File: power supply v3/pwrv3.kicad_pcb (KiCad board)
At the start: 2 copper layers, 38.3 x 37.5 mm, 56 parts, among them IC1 TLV3701IDBVR, IC2 LM25145RGYR, IC3 LMR50410YQDBVRQ1, J1 1.5 mm, J3 1933189, J4 Conn_01x04_Pin 1.27mm, Q1 35A, 30V, Q2 35A Id, 30V Vds

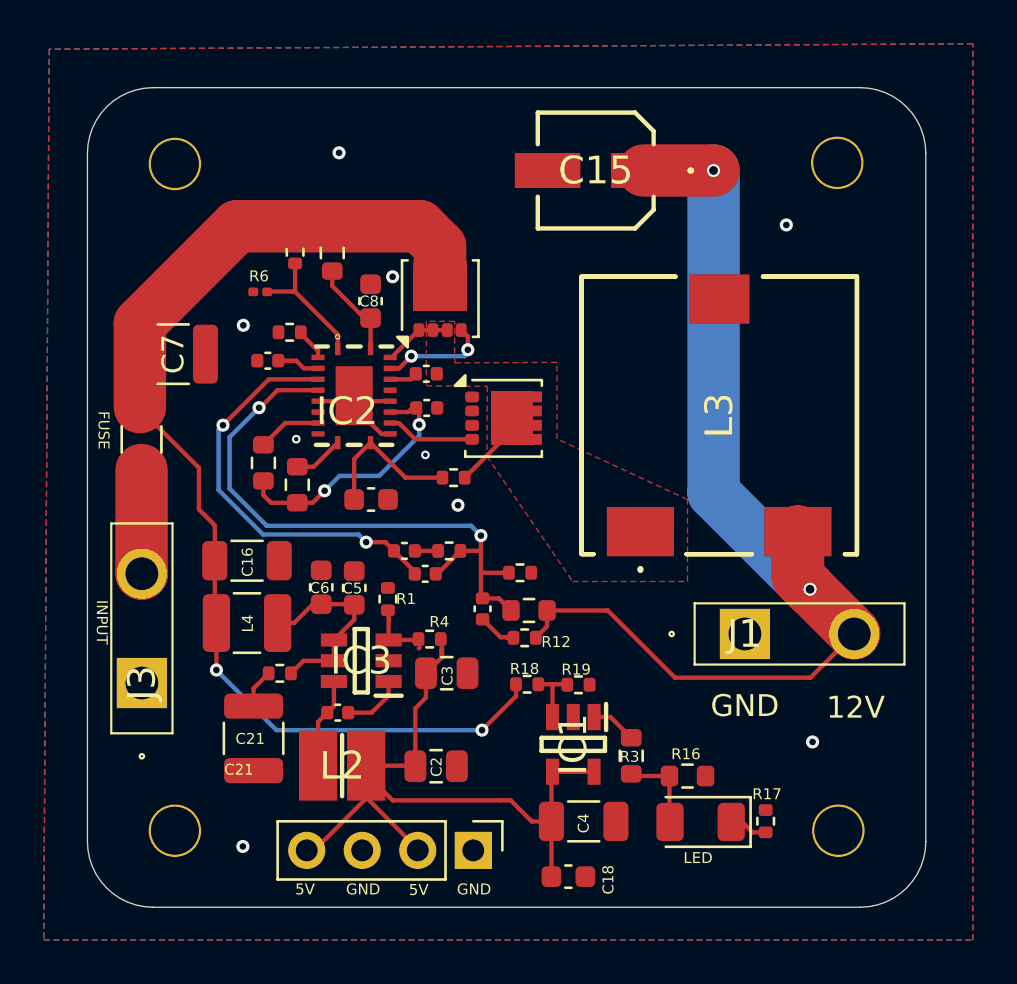
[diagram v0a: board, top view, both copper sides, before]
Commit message: capa bst updated
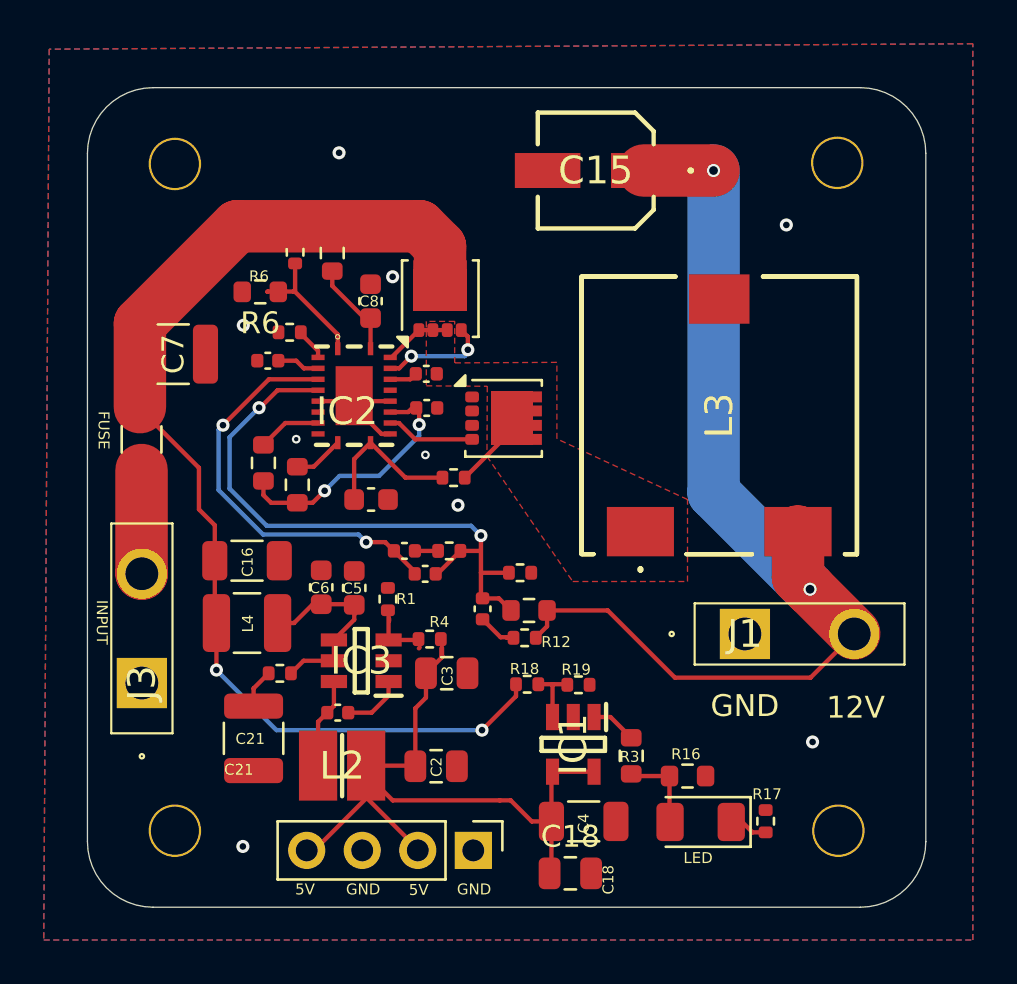
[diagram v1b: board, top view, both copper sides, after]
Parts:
- C17: value GCM1555C1H100FA16D -> 0.1uF
- C18: footprint Capacitor_SMD:C_0603_1608Metric -> Capacitor_SMD:C_0805_2012Metric
- R18: value R -> 30.9k
- R19: value R -> 22.1k
- R6: footprint Resistor_SMD:R_0201_0603Metric -> Resistor_SMD:R_0603_1608Metric
- moved C18 0.17 mm to (186.1, 110.0)
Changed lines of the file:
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@@
 			(disableapertmacros no)
 			(usegerberextensions yes)
-			(usegerberattributes yes)
-			(usegerberadvancedattributes yes)
+			(usegerberattributes no)
+			(usegerberadvancedattributes no)
 			(creategerberjobfile no)
 			(dashed_line_dash_ratio 12.000000)
@@
 			(drillshape 0)
 			(scaleselection 1)
-			(outputdirectory "gerber files/")
+			(outputdirectory "gerbers/")
 		)
 	)
@@
 			)
 		)
-		(property "Value" "R"
+		(property "Value" "22.1k"
 			(at 0 1.17 0)
 			(layer "F.Fab")
@@
 		)
 	)
-	(footprint "Resistor_SMD:R_0201_0603Metric"
+	(footprint "Resistor_SMD:R_0603_1608Metric"
 		(layer "F.Cu")
 		(at 171.905 83.35 180)
-		(descr "Resistor SMD 0201 (0603 Metric), square (rectangular) end terminal, IPC_7351 nominal, (Body size source: https://www.vishay.com/docs/20052/crcw0201e3.pdf), generated with kicad-footprint-generator")
+		(descr "Resistor SMD 0603 (1608 Metric), square (rectangular) end terminal, IPC_7351 nominal, (Body size source: IPC-SM-782 page 72, https://www.pcb-3d.com/wordpress/wp-content/uploads/ipc-sm-782a_amendment_1_and_2.pdf), generated with kicad-footprint-generator")
 		(tags "resistor")
 		(property "Reference" "R6"
-			(at 0 -1.05 0)
+			(at 0 -1.43 180)
 			(layer "F.SilkS")
-			(hide yes)
 			(effects
 				(font
@@
 		)
 		(property "Value" "8.25k"
-			(at 0 1.05 0)
+			(at 0 1.43 180)
 			(layer "F.Fab")
 			(effects
@@
 		(attr smd)
 		(fp_line
-			(start 0.7 0.35)
-			(end -0.7 0.35)
+			(start -0.237258 0.5225)
+			(end 0.237258 0.5225)
+			(stroke
+				(width 0.12)
+				(type solid)
+			)
+			(layer "F.SilkS")
+		)
+		(fp_line
+			(start -0.237258 -0.5225)
+			(end 0.237258 -0.5225)
+			(stroke
+				(width 0.12)
+				(type solid)
+			)
+			(layer "F.SilkS")
+		)
+		(fp_line
+			(start 1.48 0.73)
+			(end -1.48 0.73)
 			(stroke
 				(width 0.05)
@@
 		)
 		(fp_line
-			(start 0.7 -0.35)
-			(end 0.7 0.35)
+			(start 1.48 -0.73)
+			(end 1.48 0.73)
 			(stroke
 				(width 0.05)
@@
 		)
 		(fp_line
-			(start -0.7 0.35)
-			(end -0.7 -0.35)
+			(start -1.48 0.73)
+			(end -1.48 -0.73)
 			(stroke
 				(width 0.05)
@@
 		)
 		(fp_line
-			(start -0.7 -0.35)
-			(end 0.7 -0.35)
+			(start -1.48 -0.73)
+			(end 1.48 -0.73)
 			(stroke
 				(width 0.05)
@@
 		)
 		(fp_line
-			(start 0.3 0.15)
-			(end -0.3 0.15)
+			(start 0.8 0.4125)
+			(end -0.8 0.4125)
 			(stroke
 				(width 0.1)
@@
 		)
 		(fp_line
-			(start 0.3 -0.15)
-			(end 0.3 0.15)
+			(start 0.8 -0.4125)
+			(end 0.8 0.4125)
 			(stroke
 				(width 0.1)
@@
 		)
 		(fp_line
-			(start -0.3 0.15)
-			(end -0.3 -0.15)
+			(start -0.8 0.4125)
+			(end -0.8 -0.4125)
 			(stroke
 				(width 0.1)
@@
 		)
 		(fp_line
-			(start -0.3 -0.15)
-			(end 0.3 -0.15)
+			(start -0.8 -0.4125)
+			(end 0.8 -0.4125)
 			(stroke
 				(width 0.1)
@@
 		)
 		(fp_text user "${REFERENCE}"
-			(at 0 -0.68 0)
+			(at 0 0 180)
 			(layer "F.Fab")
 			(effects
 				(font
-					(size 0.25 0.25)
-					(thickness 0.04)
+					(size 0.4 0.4)
+					(thickness 0.06)
 				)
 			)
 		)
-		(pad "" smd roundrect
-			(at -0.345 0 180)
-			(size 0.318 0.36)
-			(layers "F.Paste")
-			(roundrect_rratio 0.25)
-		)
-		(pad "" smd roundrect
-			(at 0.345 0 180)
-			(size 0.318 0.36)
-			(layers "F.Paste")
-			(roundrect_rratio 0.25)
-		)
 		(pad "1" smd roundrect
-			(at -0.32 0 180)
-			(size 0.46 0.4)
-			(layers "F.Cu" "F.Mask")
+			(at -0.825 0 180)
+			(size 0.8 0.95)
+			(layers "F.Cu" "F.Mask" "F.Paste")
 			(roundrect_rratio 0.25)
 			(net 21 "Net-(IC2-EN{slash}UVLO)")
@@
 		)
 		(pad "2" smd roundrect
-			(at 0.32 0 180)
-			(size 0.46 0.4)
-			(layers "F.Cu" "F.Mask")
+			(at 0.825 0 180)
+			(size 0.8 0.95)
+			(layers "F.Cu" "F.Mask" "F.Paste")
 			(roundrect_rratio 0.25)
 			(net 2 "GND")
@@
 		)
 		(embedded_fonts no)
-		(model "${KICAD9_3DMODEL_DIR}/Resistor_SMD.3dshapes/R_0201_0603Metric.wrl"
+		(model "${KICAD9_3DMODEL_DIR}/Resistor_SMD.3dshapes/R_0603_1608Metric.wrl"
 			(offset
 				(xyz 0 0 0)
@@
 			)
 		)
-		(property "Value" "R"
+		(property "Value" "30.9k"
 			(at 0 1.17 0)
 			(layer "F.Fab")
@@
 		)
 	)
-	(footprint "Capacitor_SMD:C_0603_1608Metric"
+	(footprint "Capacitor_SMD:C_0805_2012Metric"
 		(layer "F.Cu")
-		(at 186 110.1)
-		(descr "Capacitor SMD 0603 (1608 Metric), square (rectangular) end terminal, IPC_7351 nominal, (Body size source: IPC-SM-782 page 76, https://www.pcb-3d.com/wordpress/wp-content/uploads/ipc-sm-782a_amendment_1_and_2.pdf), generated with kicad-footprint-generator")
+		(at 186.09 109.95)
+		(descr "Capacitor SMD 0805 (2012 Metric), square (rectangular) end terminal, IPC_7351 nominal, (Body size source: IPC-SM-782 page 76, https://www.pcb-3d.com/wordpress/wp-content/uploads/ipc-sm-782a_amendment_1_and_2.pdf, https://docs.google.com/spreadsheets/d/1BsfQQcO9C6DZCsRaXUlFlo91Tg2WpOkGARC1WS5S8t0/edit?usp=sharing), generated with kicad-footprint-generator")
 		(tags "capacitor")
 		(property "Reference" "C18"
-			(at 0 -1.43 0)
+			(at 0 -1.68 0)
 			(layer "F.SilkS")
-			(hide yes)
 			(effects
 				(font
@@
 		)
 		(property "Value" "10uF"
-			(at 0 1.43 0)
+			(at 0 1.68 0)
 			(layer "F.Fab")
 			(effects
@@
 		(attr smd)
 		(fp_line
-			(start -0.14058 -0.51)
-			(end 0.14058 -0.51)
+			(start -0.261252 -0.735)
+			(end 0.261252 -0.735)
 			(stroke
 				(width 0.12)
@@
 		)
 		(fp_line
-			(start -0.14058 0.51)
-			(end 0.14058 0.51)
+			(start -0.261252 0.735)
+			(end 0.261252 0.735)
 			(stroke
 				(width 0.12)
@@
 		)
 		(fp_line
-			(start -1.48 -0.73)
-			(end 1.48 -0.73)
+			(start -1.7 -0.98)
+			(end 1.7 -0.98)
 			(stroke
 				(width 0.05)
@@
 		)
 		(fp_line
-			(start -1.48 0.73)
-			(end -1.48 -0.73)
+			(start -1.7 0.98)
+			(end -1.7 -0.98)
 			(stroke
 				(width 0.05)
@@
 		)
 		(fp_line
-			(start 1.48 -0.73)
-			(end 1.48 0.73)
+			(start 1.7 -0.98)
+			(end 1.7 0.98)
 			(stroke
 				(width 0.05)
@@
 		)
 		(fp_line
-			(start 1.48 0.73)
-			(end -1.48 0.73)
+			(start 1.7 0.98)
+			(end -1.7 0.98)
 			(stroke
 				(width 0.05)
@@
 		)
 		(fp_line
-			(start -0.8 -0.4)
-			(end 0.8 -0.4)
+			(start -1 -0.625)
+			(end 1 -0.625)
 			(stroke
 				(width 0.1)
@@
 		)
 		(fp_line
-			(start -0.8 0.4)
-			(end -0.8 -0.4)
+			(start -1 0.625)
+			(end -1 -0.625)
 			(stroke
 				(width 0.1)
@@
 		)
 		(fp_line
-			(start 0.8 -0.4)
-			(end 0.8 0.4)
+			(start 1 -0.625)
+			(end 1 0.625)
 			(stroke
 				(width 0.1)
@@
 		)
 		(fp_line
-			(start 0.8 0.4)
-			(end -0.8 0.4)
+			(start 1 0.625)
+			(end -1 0.625)
 			(stroke
 				(width 0.1)
@@
 			(effects
 				(font
-					(size 0.4 0.4)
-					(thickness 0.06)
+					(size 0.5 0.5)
+					(thickness 0.08)
 				)
 			)
 		)
 		(pad "1" smd roundrect
-			(at -0.775 0)
-			(size 0.9 0.95)
+			(at -0.95 0)
+			(size 1 1.45)
 			(layers "F.Cu" "F.Mask" "F.Paste")
 			(roundrect_rratio 0.25)
@@
 		)
 		(pad "2" smd roundrect
-			(at 0.775 0)
-			(size 0.9 0.95)
+			(at 0.95 0)
+			(size 1 1.45)
 			(layers "F.Cu" "F.Mask" "F.Paste")
 			(roundrect_rratio 0.25)
@@
 		)
 		(embedded_fonts no)
-		(model "${KICAD9_3DMODEL_DIR}/Capacitor_SMD.3dshapes/C_0603_1608Metric.wrl"
+		(model "${KICAD9_3DMODEL_DIR}/Capacitor_SMD.3dshapes/C_0805_2012Metric.wrl"
 			(offset
 				(xyz 0 0 0)
@@
 			)
 		)
-		(property "Value" "GCM1555C1H100FA16D"
+		(property "Value" "0.1uF"
 			(at 0 1.16 0)
 			(layer "F.Fab")
